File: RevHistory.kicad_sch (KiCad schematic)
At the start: 0 parts

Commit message: Update sch v1.0
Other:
- note added: "- Changed DAC's PinHeader to FFC-4 P0.5 Connector"
- note added: "- Changed Input and Output Connectors from 6 PIN to 2x(4 PIN)"
- note removed: "- Changed Input and Output Connectors from 6 PIN to 2x(4 PIN) matched ATX12V"
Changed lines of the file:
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@@
+		)
+	)
+	(text "- Changed DAC's PinHeader to FFC-4 P0.5 Connector"
+		(exclude_from_sim no)
+		(at 41.91 100.33 0)
+		(effects
+			(font
+				(face "Arial")
+				(size 1.905 1.905)
+			)
+			(justify left)
 		)
 	)
@@
 		)
 	)
-	(text "- Changed Input and Output Connectors from 6 PIN to 2x(4 PIN) matched ATX12V"
+	(text "- Changed Input and Output Connectors from 6 PIN to 2x(4 PIN) "
 		(exclude_from_sim no)
 		(at 41.91 90.17 0)
@@
 	(text "- Removed Temp. Sensor"
 		(exclude_from_sim no)
-		(at 41.91 100.33 0)
+		(at 41.91 105.41 0)
 		(effects
 			(font

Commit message: Updated Schematic v1.0
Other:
- note added: "- (03/06/2026) PC Board is Released"
- note added: "- (18/05/2026) Initialize the project"
- note removed: "- Added 2x(47uF Polymer Cap.) on Output State"
- note removed: "- Added Input Current Sensor on Power State"
- note removed: "- Added Rsense on Input Terminal in Power Supplies Circuits"
- note removed: "- Added Series Termination resistor on HRTIM's Line"
- note removed: "- Added Turn-Off Diode in parallel with R-Gate in Gate Driver Circuits"
- note removed: "- Changed DAC's PinHeader to FFC-4 P0.5 Connector"
- note removed: "- Changed GPIO's PinHeader to FFC-16 P0.5 Connector"
- note removed: "- Changed Input and Output Connectors from 6 PIN to 2x(4 PIN)"
- note removed: "- First Version of Schematic (Printed)"
- note removed: "- Removed Temp. Sensor"
- note removed: "18/05/2026"
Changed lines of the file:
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@@
 		(comment 1 "Revision History")
 	)
-	(text "18/05/2026"
-		(exclude_from_sim no)
-		(at 151.13 50.8 0)
-		(effects
-			(font
-				(size 2.54 2.54)
-				(bold yes)
-			)
-			(justify right)
-		)
-	)
-	(text "- Added Turn-Off Diode in parallel with R-Gate in Gate Driver Circuits"
-		(exclude_from_sim no)
-		(at 41.91 80.01 0)
-		(effects
-			(font
-				(face "Arial")
-				(size 1.905 1.905)
-			)
-			(justify left)
-		)
-	)
-	(text "- Changed DAC's PinHeader to FFC-4 P0.5 Connector"
-		(exclude_from_sim no)
-		(at 41.91 100.33 0)
-		(effects
-			(font
-				(face "Arial")
-				(size 1.905 1.905)
-			)
-			(justify left)
-		)
-	)
-	(text "- Changed GPIO's PinHeader to FFC-16 P0.5 Connector"
-		(exclude_from_sim no)
-		(at 41.91 95.25 0)
-		(effects
-			(font
-				(face "Arial")
-				(size 1.905 1.905)
-			)
-			(justify left)
-		)
-	)
-	(text "- Added Input Current Sensor on Power State"
-		(exclude_from_sim no)
-		(at 41.91 74.93 0)
-		(effects
-			(font
-				(face "Arial")
-				(size 1.905 1.905)
-			)
-			(justify left)
-		)
-	)
-	(text "- First Version of Schematic (Printed)"
+	(text "- (18/05/2026) Initialize the project"
 		(exclude_from_sim no)
 		(at 41.91 59.69 0)
@@
 		)
 	)
-	(text "- Added Series Termination resistor on HRTIM's Line"
-		(exclude_from_sim no)
-		(at 41.91 85.09 0)
-		(effects
-			(font
-				(face "Arial")
-				(size 1.905 1.905)
-			)
-			(justify left)
-		)
-	)
-	(text "- Added Rsense on Input Terminal in Power Supplies Circuits"
-		(exclude_from_sim no)
-		(at 41.91 69.85 0)
-		(effects
-			(font
-				(face "Arial")
-				(size 1.905 1.905)
-			)
-			(justify left)
-		)
-	)
 	(text "Revison 1.0"
 		(exclude_from_sim no)
@@
 		)
 	)
-	(text "- Changed Input and Output Connectors from 6 PIN to 2x(4 PIN) "
-		(exclude_from_sim no)
-		(at 41.91 90.17 0)
-		(effects
-			(font
-				(face "Arial")
-				(size 1.905 1.905)
-			)
-			(justify left)
-		)
-	)
-	(text "- Removed Temp. Sensor"
-		(exclude_from_sim no)
-		(at 41.91 105.41 0)
-		(effects
-			(font
-				(face "Arial")
-				(size 1.905 1.905)
-			)
-			(justify left)
-		)
-	)
-	(text "- Added 2x(47uF Polymer Cap.) on Output State"
+	(text "- (03/06/2026) PC Board is Released "
 		(exclude_from_sim no)
 		(at 41.91 64.77 0)
@@
 		)
 		(stroke
-			(width 0.381)
-			(type default)
-		)
-	)
-	(polyline
-		(pts
-			(xy 38.1 45.72) (xy 152.4 45.72)
-		)
-		(stroke

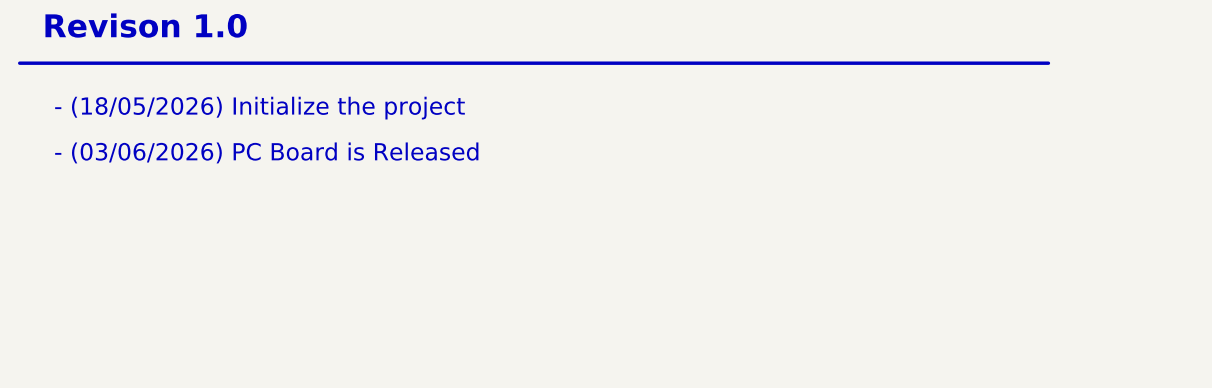
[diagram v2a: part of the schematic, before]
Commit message: Rev1.1
- Removed the Mosfet that Enable the ICs Gate Driver (p.1)
- Changed ADC input Capacitor 47pF to 1nF. (p.6
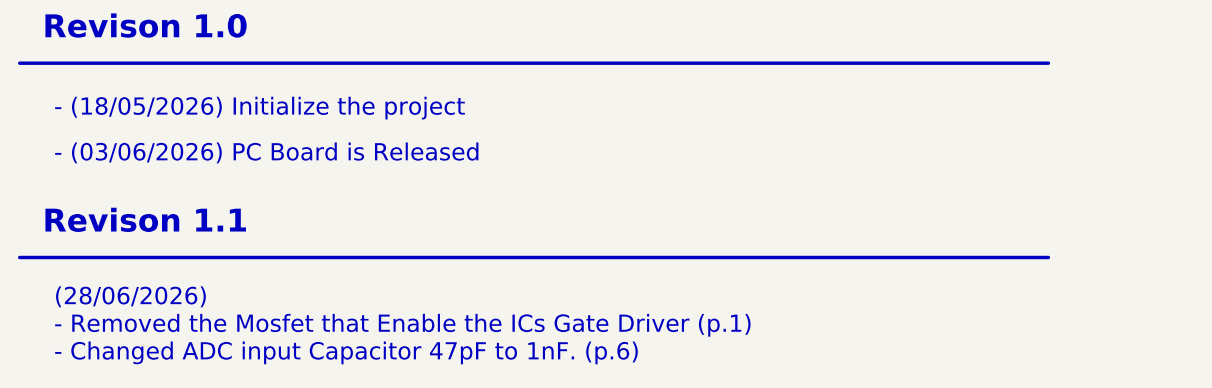
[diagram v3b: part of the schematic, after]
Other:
- note added: "(28/06/2026) - Removed the Mosfet that Enable the ICs Gate Driver (p.1) - Changed ADC input Capacitor 47pF to 1nF. (p.6)"
- note added: "Revison 1.1"
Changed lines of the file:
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@@
 	(paper "A3")
 	(title_block
-		(rev "1.0")
+		(rev "1.1")
 		(comment 1 "Revision History")
+	)
+	(text "(28/06/2026) \n- Removed the Mosfet that Enable the ICs Gate Driver (p.1)\n- Changed ADC input Capacitor 47pF to 1nF. (p.6)"
+		(exclude_from_sim no)
+		(at 41.91 83.82 0)
+		(effects
+			(font
+				(face "Arial")
+				(size 1.905 1.905)
+			)
+			(justify left)
+		)
 	)
 	(text "- (18/05/2026) Initialize the project"
@@
 				(bold yes)
 			)
+		)
+	)
+	(text "Revison 1.1"
+		(exclude_from_sim no)
+		(at 40.64 72.39 0)
+		(effects
+			(font
+				(size 2.54 2.54)
+				(bold yes)
+			)
+			(justify left)
 		)
 	)
@@
 		)
 	)
+	(polyline
+		(pts
+			(xy 38.1 76.2) (xy 152.4 76.2)
+		)
+		(stroke
+			(width 0.381)
+			(type default)
+		)
+	)
